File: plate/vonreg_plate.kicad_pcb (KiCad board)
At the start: 2 copper layers, 99.1 x 81.3 mm, 0 parts

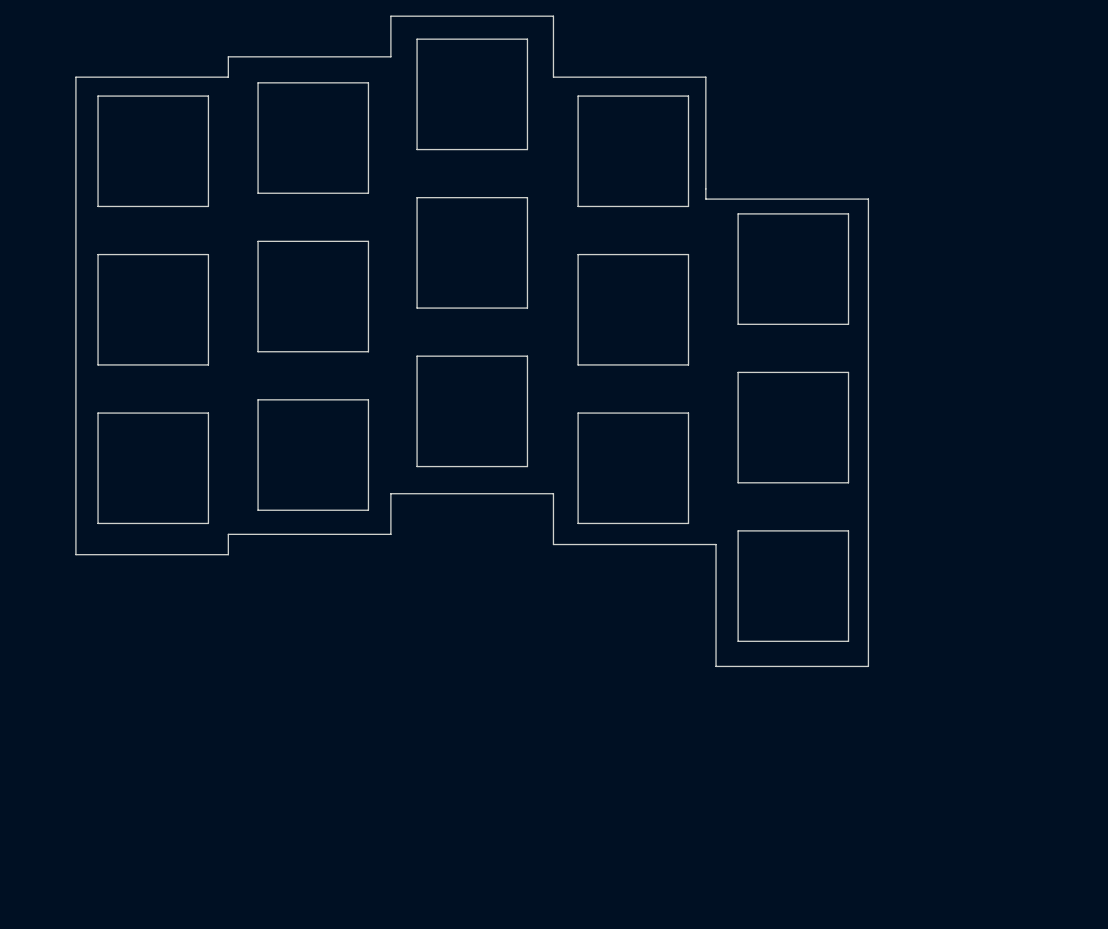
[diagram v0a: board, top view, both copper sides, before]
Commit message: top plate: increase margins
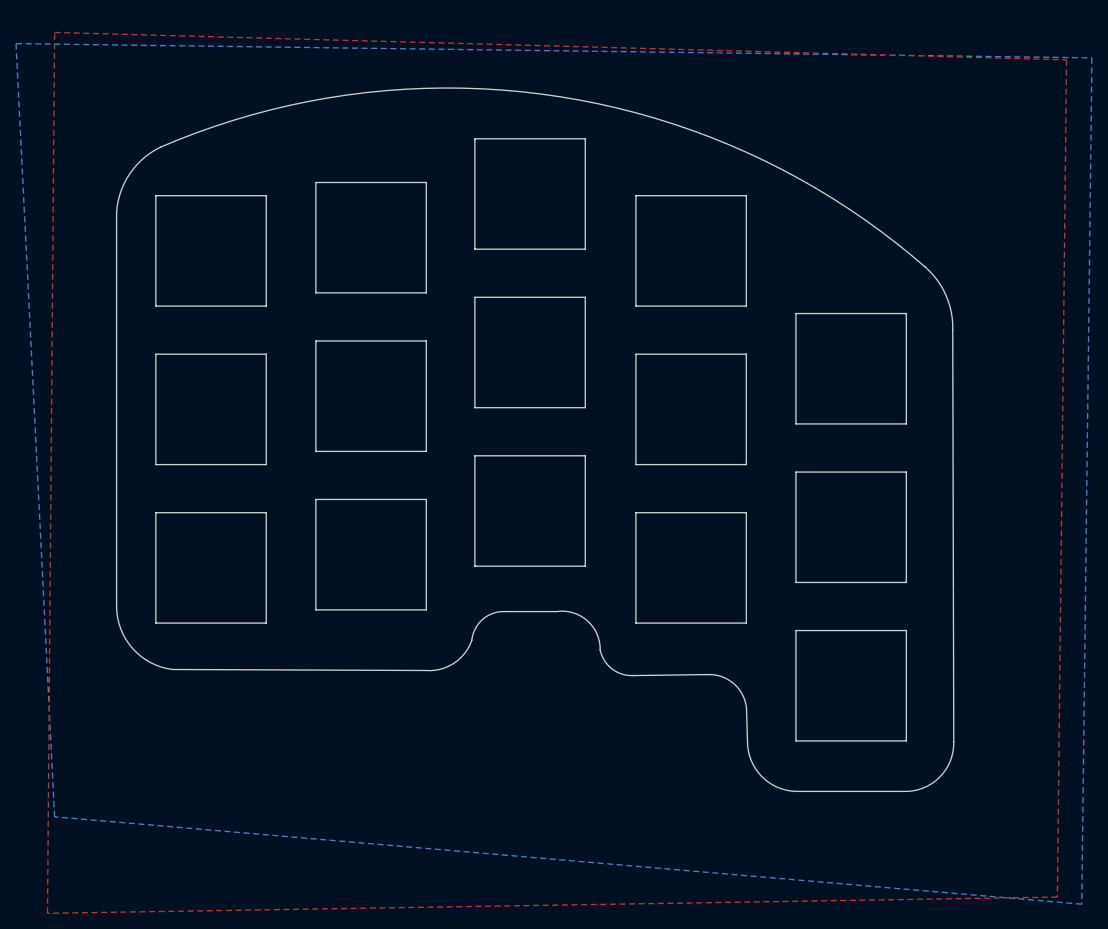
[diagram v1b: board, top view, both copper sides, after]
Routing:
- added copper zone on B.Cu, net (none)
- added copper zone on F.Cu, net (none)
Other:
- board size 99.1 x 81.3 mm -> 104.6 x 87.9 mm
